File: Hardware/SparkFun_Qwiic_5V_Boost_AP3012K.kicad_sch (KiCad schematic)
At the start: 34 parts, among them J1 Qwiic_RA, J2 Qwiic_RA, J3 Conn_01x06, Q1 BSS138, Q2 BSS138, U1 AP3012

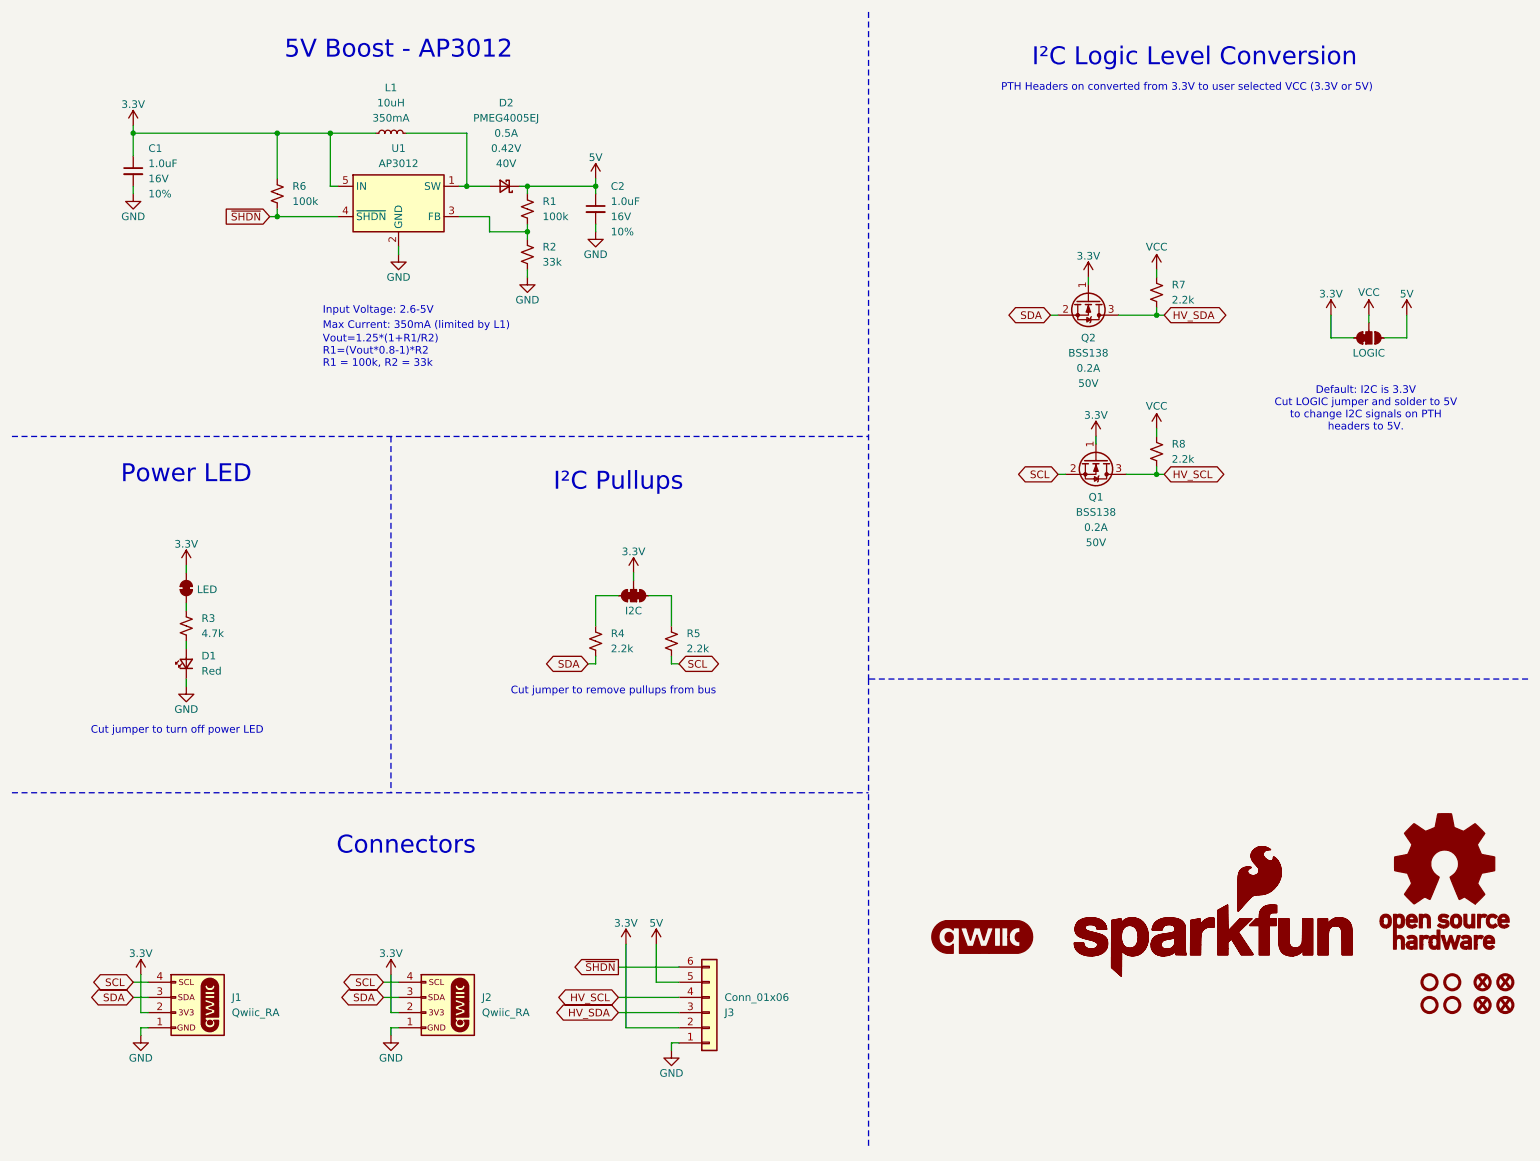
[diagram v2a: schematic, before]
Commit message: more design review feedback
-SCH, changed all flags to inputs
-BRD, re-routed HV I2C lines to avoid coupling with 3V3 trace
-BRD, adjusted 5V and SHDN routing for less vias/more-direct
-BRD, adjusted SDA/SCL routing away from right qwiic connector to provide more clearance from mask.
-BRD, removed and moved GND vias to avoid bottom silk
-BRD, scooted GND vias near SDA/SCL header pins to avoid bulging in the pours.
-BRD, updated layers to new standards
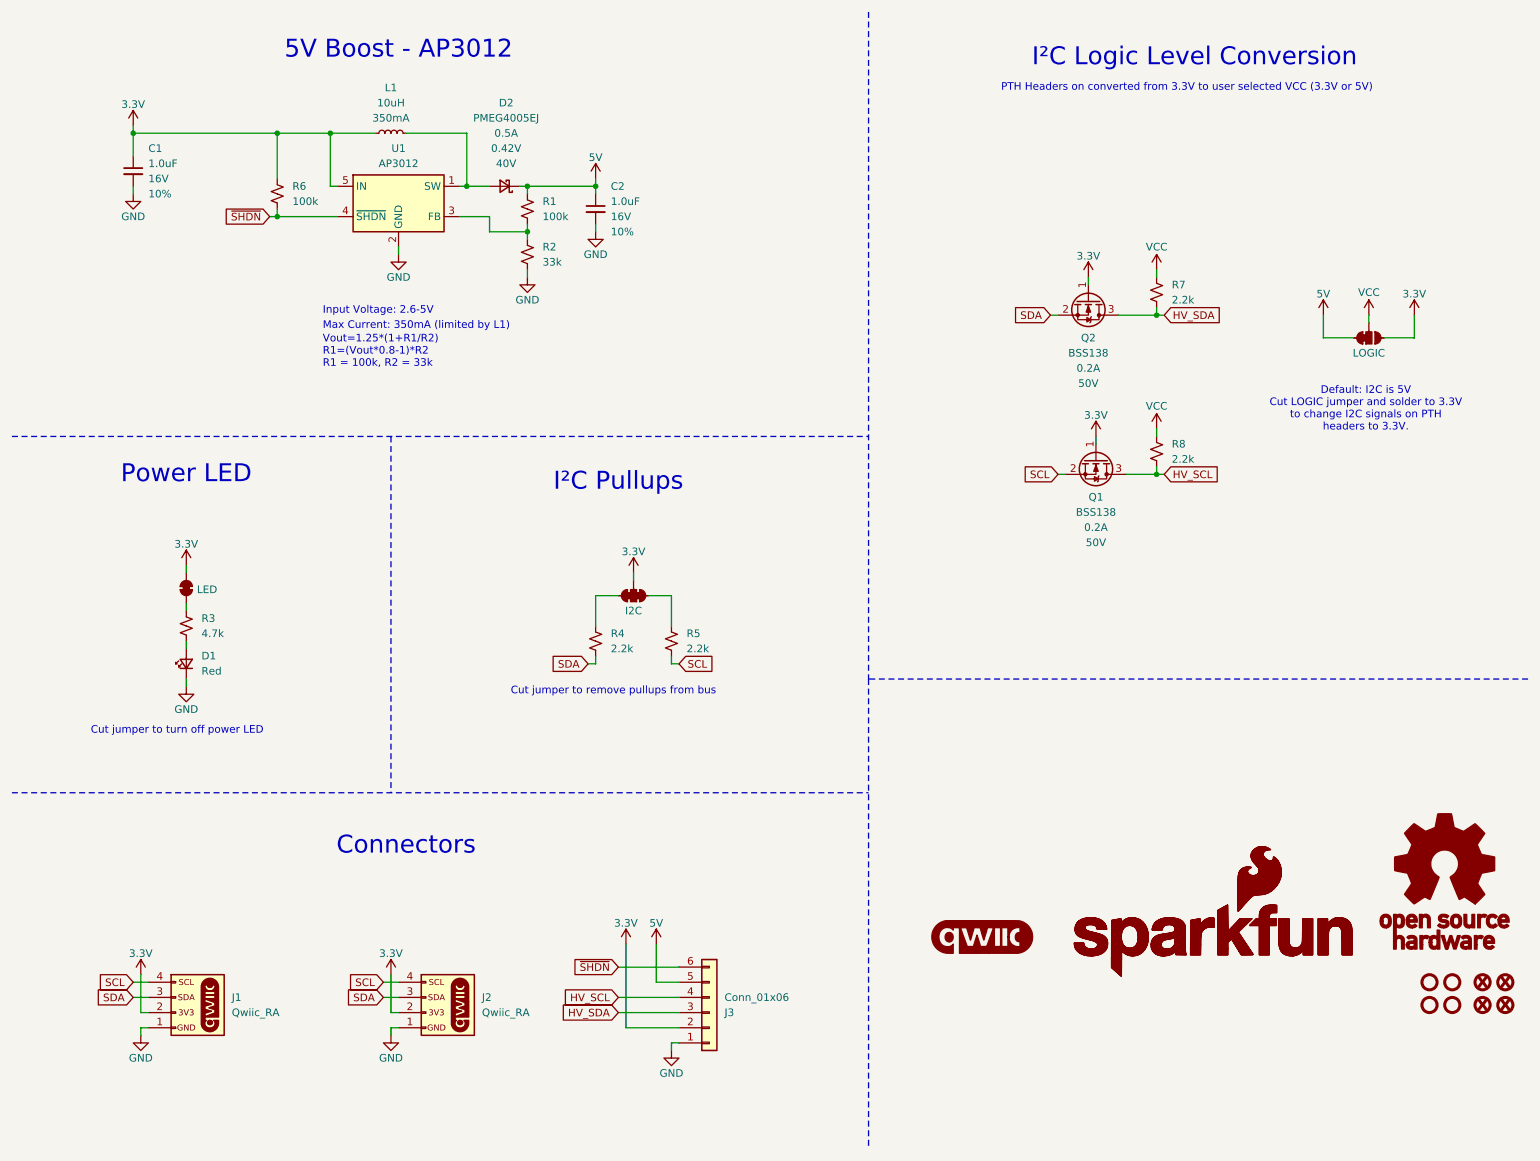
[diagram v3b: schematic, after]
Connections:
- net 3.3V: now also JP3.3 (C); no longer JP3.1 (A)
- net 5V: now also JP3.1 (A); no longer JP3.3 (C)
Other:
- note added: "Default: I2C is 5V Cut LOGIC jumper and solder to 3.3V to change I2C signals on PTH headers to 3.3V."
- note removed: "Default: I2C is 3.3V Cut LOGIC jumper and solder to 5V to change I2C signals on PTH headers to 5V."
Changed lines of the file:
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@@
 	(wire
 		(pts
+			(xy 237.49 67.31) (xy 232.41 67.31)
+		)
+		(stroke
+			(width 0)
+			(type default)
+		)
+	)
+	(wire
+		(pts
 			(xy 57.15 33.02) (xy 57.15 40.64)
 		)
@@
 	(wire
 		(pts
-			(xy 242.57 67.31) (xy 246.38 67.31)
+			(xy 242.57 67.31) (xy 247.65 67.31)
 		)
 		(stroke
@@
 		)
 	)
-	(wire
-		(pts
-			(xy 233.68 63.5) (xy 233.68 67.31)
-		)
-		(stroke
-			(width 0)
-			(type default)
-		)
-	)
 	(polyline
 		(pts
@@
 	(wire
 		(pts
-			(xy 246.38 63.5) (xy 246.38 67.31)
-		)
-		(stroke
-			(width 0)
-			(type default)
-		)
-	)
-	(wire
-		(pts
 			(xy 67.31 41.91) (xy 66.04 41.91)
 		)
@@
 	(wire
 		(pts
-			(xy 237.49 67.31) (xy 233.68 67.31)
+			(xy 247.65 67.31) (xy 247.65 63.5)
 		)
 		(stroke
@@
 	(wire
 		(pts
+			(xy 232.41 67.31) (xy 232.41 63.5)
+		)
+		(stroke
+			(width 0)
+			(type default)
+		)
+	)
+	(wire
+		(pts
 			(xy 88.9 41.91) (xy 87.63 41.91)
 		)
@@
 		)
 	)
-	(text "Default: I2C is 3.3V\nCut LOGIC jumper and solder to 5V\nto change I2C signals on PTH \nheaders to 5V."
+	(text "Default: I2C is 5V\nCut LOGIC jumper and solder to 3.3V\nto change I2C signals on PTH \nheaders to 3.3V."
 		(exclude_from_sim no)
 		(at 239.522 79.248 0)
@@
 	)
 	(global_label "HV_SDA"
-		(shape bidirectional)
+		(shape input)
 		(at 114.3 180.34 180)
 		(fields_autoplaced yes)
@@
 	)
 	(global_label "HV_SCL"
-		(shape bidirectional)
+		(shape input)
 		(at 205.74 90.17 0)
 		(fields_autoplaced yes)
@@
 		)
 		(property "Intersheetrefs" "${INTERSHEET_REFS}"
-			(at 216.7308 90.17 0)
+			(at 215.6195 90.17 0)
 			(effects
 				(font
@@
 	)
 	(global_label "SCL"
-		(shape bidirectional)
+		(shape input)
 		(at 124.46 121.92 0)
 		(fields_autoplaced yes)
@@
 	)
 	(global_label "HV_SCL"
-		(shape bidirectional)
+		(shape input)
 		(at 114.3 177.8 180)
 		(fields_autoplaced yes)
@@
 	)
 	(global_label "SDA"
-		(shape bidirectional)
+		(shape input)
 		(at 74.93 177.8 180)
 		(fields_autoplaced yes)
@@
 	)
 	(global_label "SDA"
-		(shape bidirectional)
+		(shape input)
 		(at 109.22 121.92 180)
 		(fields_autoplaced yes)
@@
 	)
 	(global_label "HV_SDA"
-		(shape bidirectional)
+		(shape input)
 		(at 205.74 63.5 0)
 		(fields_autoplaced yes)
@@
 		)
 		(property "Intersheetrefs" "${INTERSHEET_REFS}"
-			(at 216.7913 63.5 0)
+			(at 215.68 63.5 0)
 			(effects
 				(font
@@
 	)
 	(global_label "SDA"
-		(shape bidirectional)
+		(shape input)
 		(at 186.69 63.5 180)
 		(fields_autoplaced yes)
@@
 	)
 	(global_label "SCL"
-		(shape bidirectional)
+		(shape input)
 		(at 33.02 175.26 180)
 		(fields_autoplaced yes)
@@
 	)
 	(global_label "SCL"
-		(shape bidirectional)
+		(shape input)
 		(at 74.93 175.26 180)
 		(fields_autoplaced yes)
@@
 	)
 	(global_label "SDA"
-		(shape bidirectional)
+		(shape input)
 		(at 33.02 177.8 180)
 		(fields_autoplaced yes)
@@
 	)
 	(global_label "~{SHDN}"
-		(shape output)
+		(shape input)
 		(at 114.3 172.72 180)
 		(fields_autoplaced yes)
@@
 	)
 	(global_label "SCL"
-		(shape bidirectional)
+		(shape input)
 		(at 187.96 90.17 180)
 		(fields_autoplaced yes)
@@
 	(symbol
 		(lib_id "SparkFun-PowerSymbol:5V")
-		(at 246.38 63.5 0)
+		(at 232.41 63.5 0)
 		(unit 1)
 		(exclude_from_sim no)
@@
 		(fields_autoplaced yes)
 		(property "Reference" "#PWR07"
-			(at 246.38 67.31 0)
+			(at 232.41 67.31 0)
 			(effects
 				(font
@@
 		)
 		(property "Value" "5V"
-			(at 246.38 59.944 0)
+			(at 232.41 59.944 0)
 			(effects
 				(font
@@
 		)
 		(property "Footprint" ""
-			(at 246.38 63.5 0)
+			(at 232.41 63.5 0)
 			(effects
 				(font
@@
 		)
 		(property "Datasheet" ""
-			(at 246.38 63.5 0)
+			(at 232.41 63.5 0)
 			(effects
 				(font
@@
 		)
 		(property "Description" "Power symbol creates a global label with name \"5V\""
-			(at 246.38 63.5 0)
+			(at 232.41 63.5 0)
 			(effects
 				(font
@@
 	(symbol
 		(lib_id "SparkFun-PowerSymbol:3.3V")
-		(at 233.68 63.5 0)
+		(at 247.65 63.5 0)
 		(unit 1)
 		(exclude_from_sim no)
@@
 		(dnp no)
 		(property "Reference" "#PWR06"
-			(at 233.68 67.31 0)
+			(at 247.65 67.31 0)
 			(effects
 				(font
@@
 		)
 		(property "Value" "3.3V"
-			(at 233.68 59.944 0)
+			(at 247.65 59.944 0)
 			(effects
 				(font
@@
 		)
 		(property "Footprint" ""
-			(at 233.68 63.5 0)
+			(at 247.65 63.5 0)
 			(effects
 				(font
@@
 		)
 		(property "Datasheet" ""
-			(at 233.68 63.5 0)
+			(at 247.65 63.5 0)
 			(effects
 				(font
@@
 		)
 		(property "Description" "Power symbol creates a global label with name \"3.3V\""
-			(at 233.68 63.5 0)
+			(at 247.65 63.5 0)
 			(effects
 				(font

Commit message: I2C HV pullup jumper
-added pullup jumper for I2C HV
-Updated D2 to latest footprint
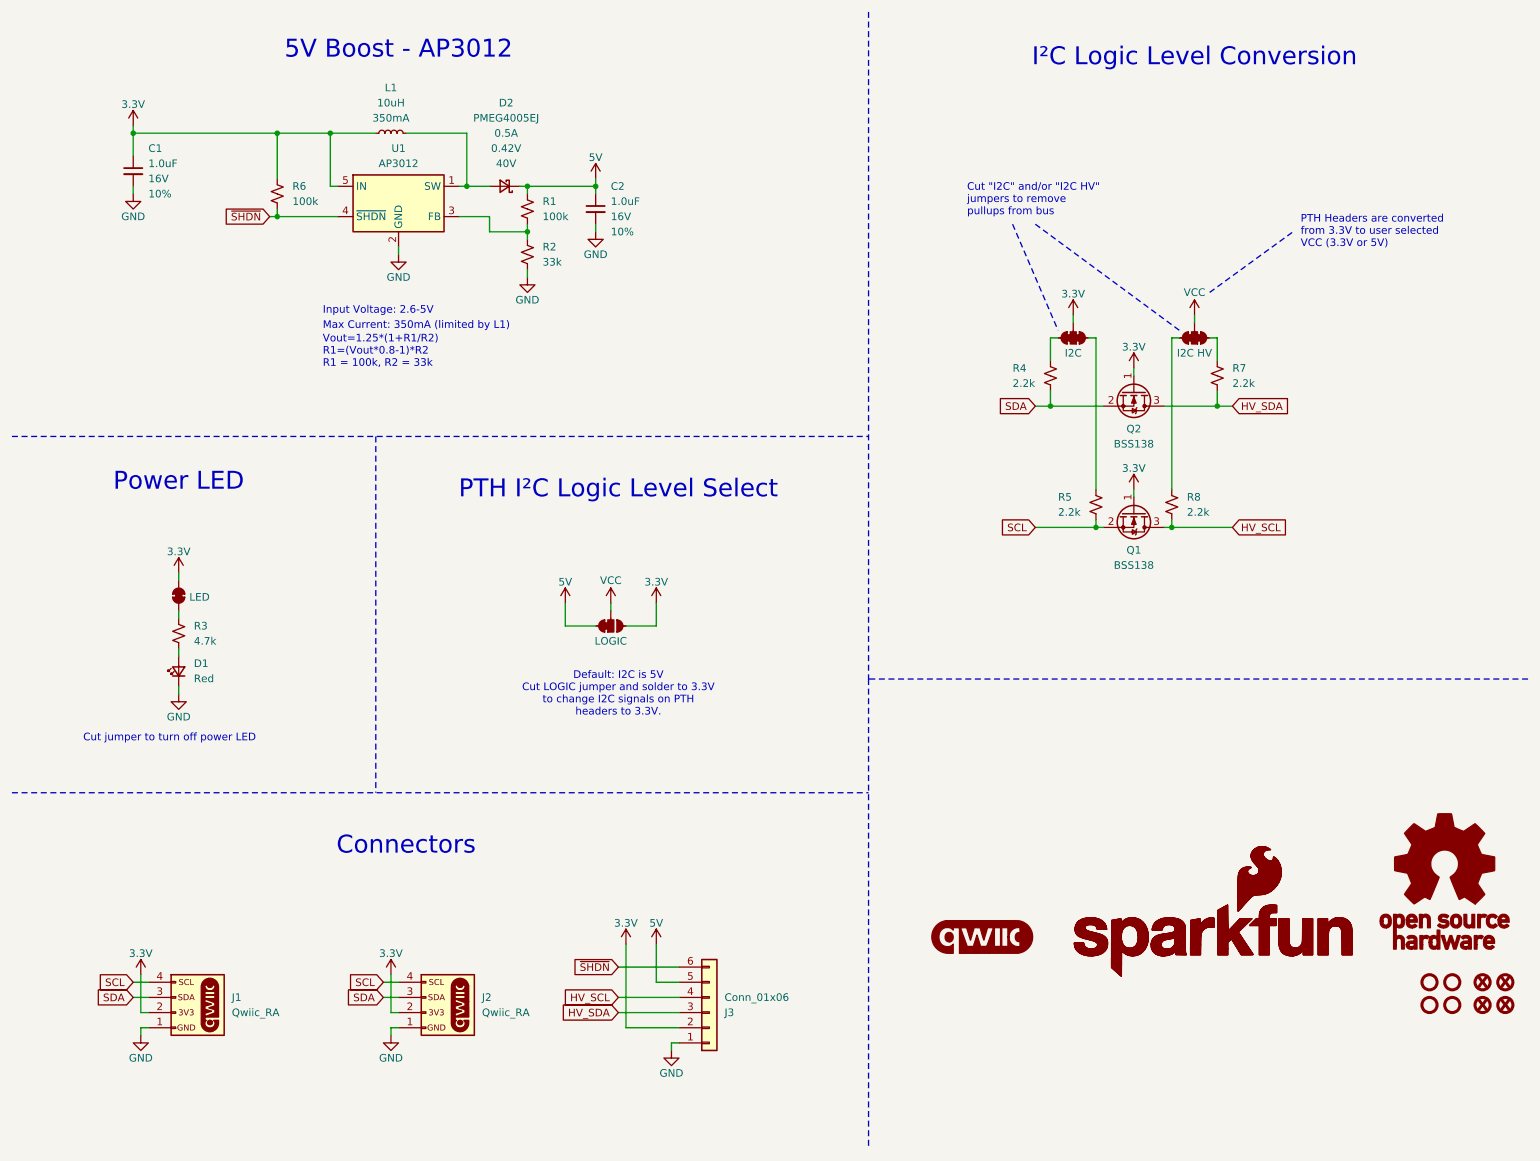
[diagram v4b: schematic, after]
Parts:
- added JP4: I2C HV, SparkFun-Jumper:Jumper_3_NC-2_Trace, symbol SparkFun-Jumper:SolderJumper_3_Bridged123
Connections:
- net 5V: now also D2.1 (K); no longer D2.C
- net VCC: now also JP4.2 (B); no longer R7.1, R8.1
- net at L1.2, U1.1 (SW): now also D2.2 (A); no longer D2.A
- new net: JP4.1 (A), R7.1
- new net: JP4.3 (C), R8.1
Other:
- note added: "Cut "I2C" and/or "I2C HV" jumpers to remove pullups from bus"
- note added: "PTH Headers are converted from 3.3V to user selected VCC (3.3V or 5V)"
- note added: "PTH I²C Logic Level Select"
- note removed: "Cut jumper to remove pullups from bus"
- note removed: "I²C Pullups"
- note removed: "PTH Headers on converted from 3.3V to user selected VCC (3.3V or 5V)"
- moved on the sheet: D1, Q1, Q2, R3, R4, R5, R7, R8

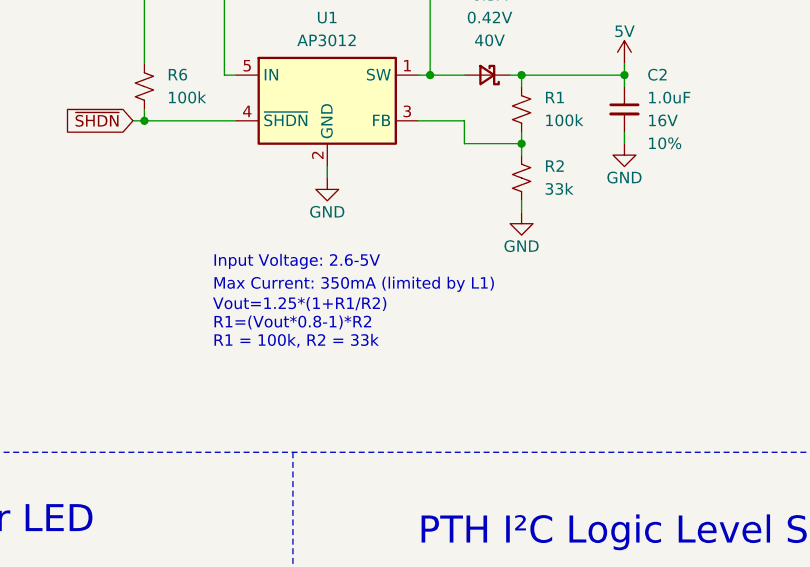
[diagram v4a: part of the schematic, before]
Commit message: final feedback
-BRD - turned on all layers to visible
-SCH - changed note about max current to 100mA
-nudged SDA trace to remove a bump
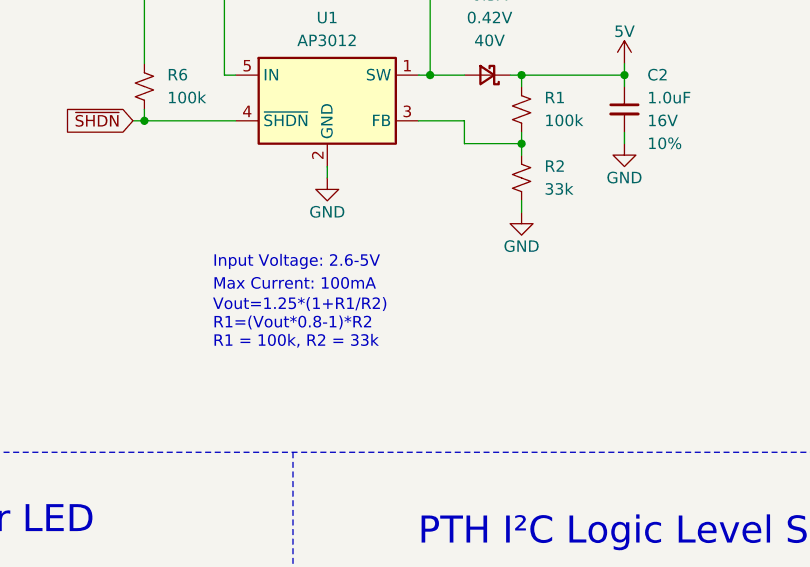
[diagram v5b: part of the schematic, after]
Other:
- note added: "Max Current: 100mA"
- note removed: "Max Current: 350mA (limited by L1)"
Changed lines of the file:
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@@
 		)
 	)
-	(text "Max Current: 350mA (limited by L1)"
+	(text "Max Current: 100mA"
 		(exclude_from_sim no)
 		(at 64.77 66.04 0)
